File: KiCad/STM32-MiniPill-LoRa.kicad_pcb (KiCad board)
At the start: 2 copper layers, 51.3 x 28.8 mm, 6 parts, among them U1 STM32L051C8Tx, U2 RFM95W-868S2

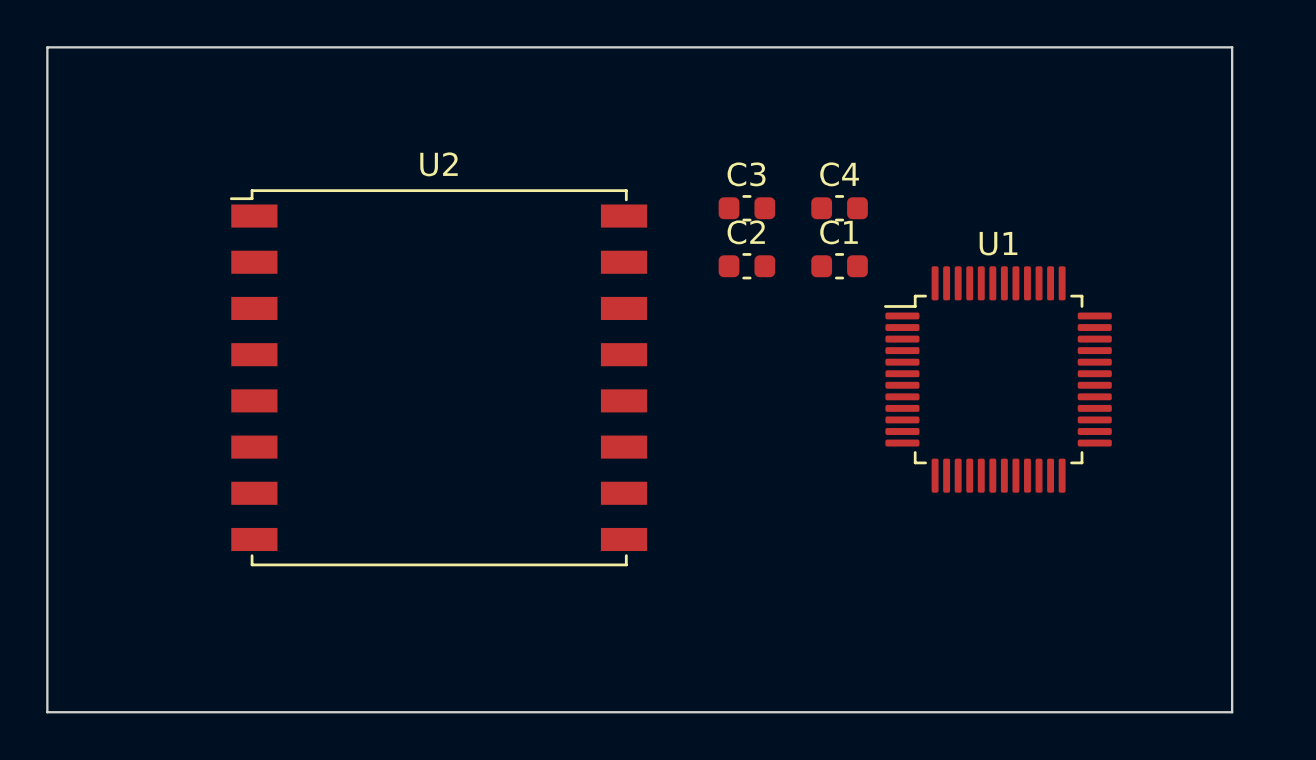
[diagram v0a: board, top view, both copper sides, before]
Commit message: adding ST-Link Connector
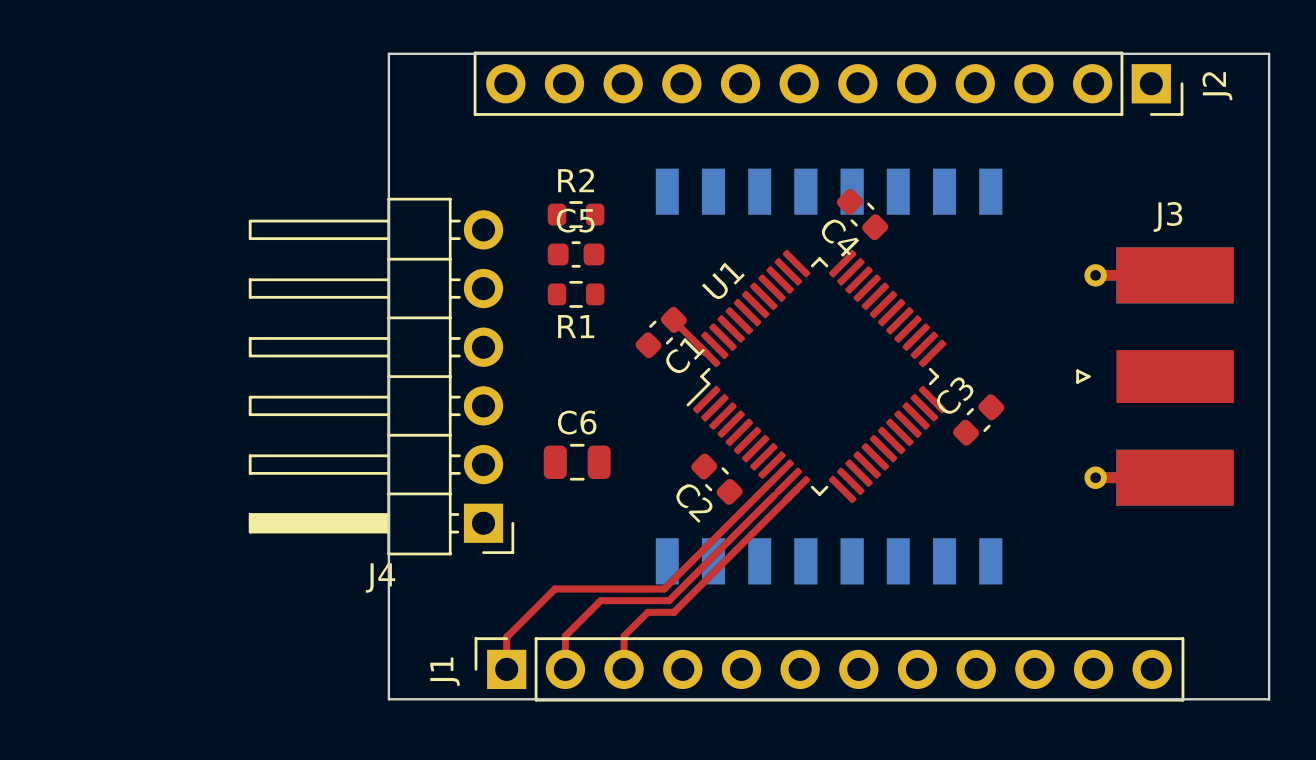
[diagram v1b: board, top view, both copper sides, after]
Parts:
- added C5: 100nF, Capacitor_SMD:C_0603_1608Metric, F.Cu at (144.6, 92.5)
- added C6: 10uF, Capacitor_SMD:C_0805_2012Metric, F.Cu at (144.7, 101.5)
- added J1: Conn_01x12_Female, Connector_PinSocket_2.54mm:PinSocket_1x12_P2.54mm_Vertical, F.Cu at (141.6, 110.5)
- added J2: Conn_01x12_Female, Connector_PinSocket_2.54mm:PinSocket_1x12_P2.54mm_Vertical, F.Cu at (169.5, 85.1)
- added J3: Conn_Coaxial, Connector_Coaxial:SMA_Molex_73251-1153_EdgeMount_Horizontal, F.Cu at (168.8, 97.8)
- added J4: Conn_01x06_Male, Connector_PinHeader_2.54mm:PinHeader_1x06_P2.54mm_Horizontal, F.Cu at (140.6, 104.1)
- added R1: 100K, Resistor_SMD:R_0603_1608Metric, F.Cu at (144.6, 94.2)
- added R2: 100K, Resistor_SMD:R_0603_1608Metric, F.Cu at (144.6, 90.8)
- C1, C2, C3, C4: value C -> 100nF
- U2: moved to B.Cu
- moved U2 16.9 mm to (155.6, 97.8), turned to -90 degrees
- moved C3 13.6 mm to (162.1, 99.7), turned to 45 degrees
- moved C2 9.31 mm to (150.7, 102.2), turned to 135 degrees
- moved C1 8.24 mm to (148.3, 95.9), turned to -135 degrees
- moved U1 7.75 mm to (155.2, 97.8), turned to 45 degrees
- moved C4 1.03 mm to (157.0, 90.8), turned to 135 degrees
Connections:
- U1 pad 10: unconnected-(U1-Pad10) -> /PA0
- U1 pad 11: unconnected-(U1-Pad11) -> /PA1
- U1 pad 12: unconnected-(U1-Pad12) -> /PA2
- U1 pad 13: unconnected-(U1-Pad13) -> /PA3
- U1 pad 14: unconnected-(U1-Pad14) -> /NSS
- U1 pad 15: unconnected-(U1-Pad15) -> /SCK
- U1 pad 16: unconnected-(U1-Pad16) -> /MISO
- U1 pad 17: unconnected-(U1-Pad17) -> /MOSI
- U1 pad 21: unconnected-(U1-Pad21) -> /PB10
- U1 pad 22: unconnected-(U1-Pad22) -> /PB11
- U1 pad 29: unconnected-(U1-Pad29) -> /PA8
- U1 pad 30: unconnected-(U1-Pad30) -> /RESET
- U1 pad 31: unconnected-(U1-Pad31) -> /DIO0
- U1 pad 34: unconnected-(U1-Pad34) -> /SWDIO
- U1 pad 37: unconnected-(U1-Pad37) -> /SWCLK
- U1 pad 40: unconnected-(U1-Pad40) -> /DIO1
- U1 pad 41: unconnected-(U1-Pad41) -> /DIO2
- U1 pad 42: unconnected-(U1-Pad42) -> /PB6
- U1 pad 43: unconnected-(U1-Pad43) -> /PB7
- U1 pad 44: unconnected-(U1-Pad44) -> Net-(R2-Pad1)
- U1 pad 45: unconnected-(U1-Pad45) -> /PB8
- U1 pad 46: unconnected-(U1-Pad46) -> /PB9
- U1 pad 7: unconnected-(U1-Pad7) -> /NRST
- U2 pad 1: unconnected-(U2-Pad1) -> GND
- U2 pad 10: unconnected-(U2-Pad10) -> GND
- U2 pad 13: unconnected-(U2-Pad13) -> +3.3V
- U2 pad 14: unconnected-(U2-Pad14) -> /DIO0
- U2 pad 15: unconnected-(U2-Pad15) -> /DIO1
- U2 pad 16: unconnected-(U2-Pad16) -> /DIO2
- U2 pad 2: unconnected-(U2-Pad2) -> /MISO
- U2 pad 3: unconnected-(U2-Pad3) -> /MOSI
- U2 pad 4: unconnected-(U2-Pad4) -> /SCK
- U2 pad 5: unconnected-(U2-Pad5) -> /NSS
- U2 pad 6: unconnected-(U2-Pad6) -> /RESET
- U2 pad 8: unconnected-(U2-Pad8) -> GND
- U2 pad 9: unconnected-(U2-Pad9) -> Net-(J3-Pad1)
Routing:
- net /PA0: track 0.00 -> 15.4 mm
- net /PA1: track 0.00 -> 13.0 mm
- net /PA2: track 0.00 -> 11.5 mm
- net +3.3V: track 0.00 -> 2.04 mm
- added copper zone on B.Cu, net GND
- added copper zone on F.Cu, net GND
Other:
- board size 51.3 x 28.8 mm -> 38.1 x 27.9 mm

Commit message: adding 3D Models of SMA Molex Connector
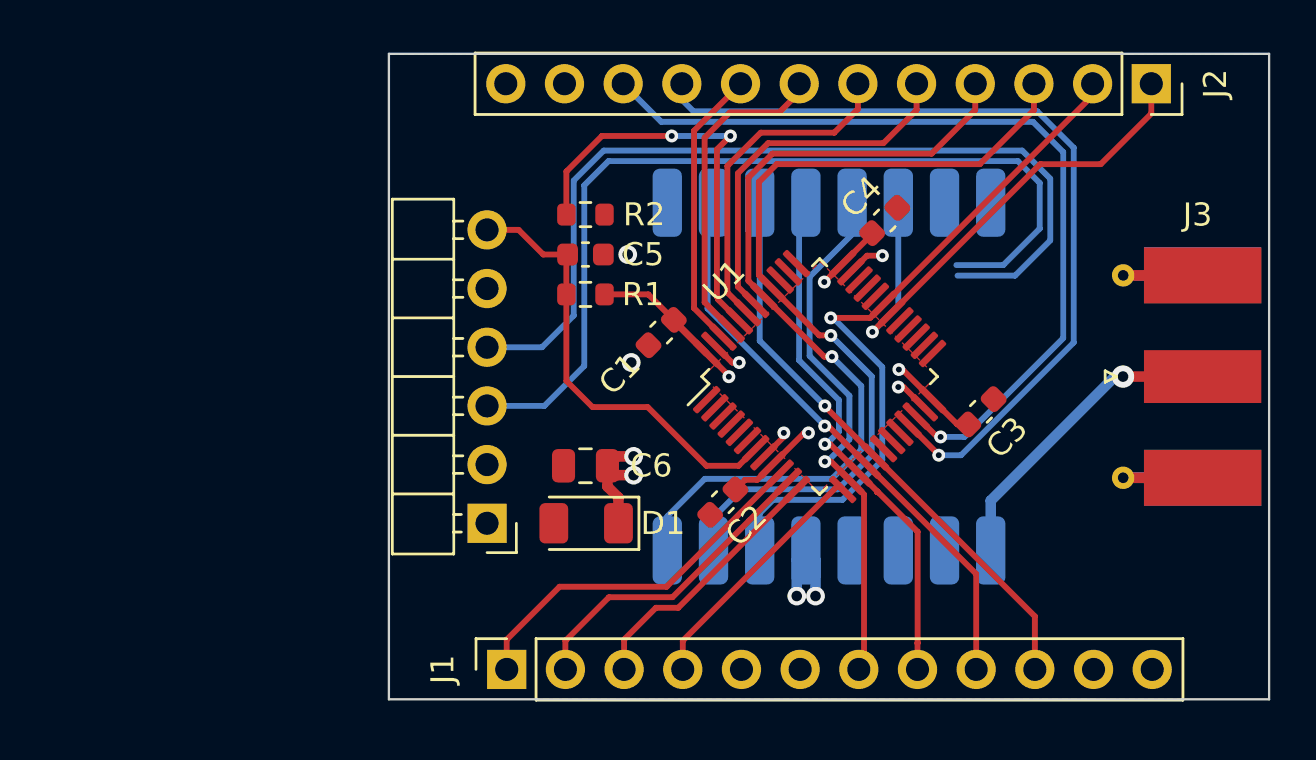
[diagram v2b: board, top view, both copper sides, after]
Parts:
- added D1: D, Diode_SMD:D_1206_3216Metric, F.Cu at (145.1, 104.1)
- moved J3 1.19 mm to (170.0, 97.8)
- moved C2 1.02 mm to (151.0, 103.2), turned to -135 degrees
- moved C4 1.00 mm to (158.0, 91.0), turned to 45 degrees
- moved C5 0.41 mm to (145.0, 92.5)
- moved R1 0.41 mm to (145.0, 94.2)
- moved R2 0.41 mm to (145.0, 90.8)
- moved C6 0.39 mm to (145.0, 101.7), turned to 180 degrees
- moved C3 0.37 mm to (162.2, 99.3)
- moved J4 0.15 mm to (140.8, 104.1)
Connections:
- J1 pad 11: VCC -> +3.3V
- J1 pad 5: VCC -> +3.3V
- J2 pad 1: /PA9 -> /RESET
- J2 pad 12: VCC -> +3.3V
- J4 pad 1: VCC -> +3.3V
- J4 pad 5: VCC -> +3.3V
- U1 pad 29: /PA8 -> unconnected-(U1-PA8-Pad29)
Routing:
- net +3.3V: track 2.04 -> 83.6 mm, vias 0 -> 8
- net /SWCLK: track 0.00 -> 39.5 mm
- net /SWDIO: track 0.00 -> 39.1 mm
- net /DIO1: track 0.00 -> 37.9 mm, vias 0 -> 1
- net /DIO2: track 0.00 -> 37.2 mm, vias 0 -> 1
- net /PB11: track 0.00 -> 36.8 mm, vias 0 -> 1
- net /PB10: track 0.00 -> 36.7 mm, vias 0 -> 1
- net /DIO0: track 0.00 -> 30.8 mm, vias 0 -> 1
- net /MISO: track 0.00 -> 25.2 mm, vias 0 -> 1
- net /MOSI: track 0.00 -> 25.1 mm, vias 0 -> 1
- net /RESET: track 0.00 -> 23.3 mm, vias 0 -> 1
- net /SCK: track 0.00 -> 23.1 mm, vias 0 -> 1
- net /NSS: track 0.00 -> 23.1 mm, vias 0 -> 1
- net /NRST: track 0.00 -> 19.4 mm
- net Net-(U1-BOOT0): track 0.00 -> 18.2 mm, vias 0 -> 2
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- added copper zone on F.Cu, net +3.3V
- added copper zone on In1.Cu, net +3.3V
- added copper zone on In2.Cu, net GND
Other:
- copper layers 2 -> 4

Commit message: first time every trace routed
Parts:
- moved C4 0.29 mm to (157.8, 90.8)
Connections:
- J1 pad 11: +3.3V -> VCC
- J1 pad 5: +3.3V -> VCC
- J2 pad 12: +3.3V -> VCC
- J4 pad 1: +3.3V -> VCC
- J4 pad 5: +3.3V -> VCC
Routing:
- net VCC: track 0.00 -> 58.9 mm, vias 0 -> 1
- net +3.3V: track 83.6 -> 27.7 mm
- net /SWCLK: track 39.5 -> 50.5 mm, vias 0 -> 1
- net GND: track 5.91 -> 11.1 mm, vias 6 -> 10
- net /PB10: track 36.7 -> 37.7 mm
- net /PB11: track 36.8 -> 37.8 mm
- net /DIO0: track 30.8 -> 31.6 mm
- net /DIO1: track 37.9 -> 37.1 mm
- net /DIO2: track 37.2 -> 36.7 mm
- net /SWDIO: track 39.1 -> 39.4 mm, vias 0 -> 1
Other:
- board text added: "A0"
- board text added: "A1"
- board text added: "A10"
- board text added: "A2"
- board text added: "A3"
- board text added: "A4"
- board text added: "A5"
- board text added: "A6"
- board text added: "A7"
- board text added: "A9"
- board text added: "B10"
- board text added: "B11"
- board text added: "B4"
- board text added: "B5"
- board text added: "B6"
- board text added: "B7"
- board text added: "B8"
- board text added: "B9"
- board text added: "GND"
- board text added: "VCC"

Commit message: last modification before push to GitHub
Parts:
- added REF**: MountingHole_2.2mm_M2_DIN965, MountingHole:MountingHole_2.2mm_M2_DIN965, F.Cu at (138.2, 110.1)
- added REF**: MountingHole_2.2mm_M2_DIN965, MountingHole:MountingHole_2.2mm_M2_DIN965, F.Cu at (173.0, 85.5)
- added REF**: MountingHole_2.2mm_M2_DIN965, MountingHole:MountingHole_2.2mm_M2_DIN965, F.Cu at (173.0, 110.1)
- added REF**: MountingHole_2.2mm_M2_DIN965, MountingHole:MountingHole_2.2mm_M2_DIN965, F.Cu at (138.2, 85.5)
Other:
- board text added: "G"
- board text added: "ST-LINK"
- board text added: "V"
- board text added: "locked"

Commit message: fist order
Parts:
- removed D1: D, Diode_SMD:D_1206_3216Metric
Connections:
- C1 pad 1: +3.3V -> VCC
- C2 pad 1: +3.3V -> VCC
- C3 pad 1: +3.3V -> VCC
- C4 pad 1: +3.3V -> VCC
- C6 pad 1: +3.3V -> VCC
- R1 pad 1: +3.3V -> VCC
- U1 pad 24: +3.3V -> VCC
- U1 pad 36: +3.3V -> VCC
- U1 pad 48: +3.3V -> VCC
- U1 pad 9: +3.3V -> VCC
- U2 pad 13: +3.3V -> VCC
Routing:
- net +3.3V: track 27.7 -> 0.00 mm, vias 8 -> 0
- net VCC: track 58.9 -> 31.7 mm, vias 1 -> 8
- added copper zone on F.Cu, net VCC
- added copper zone on In1.Cu, net VCC
- removed copper zone on F.Cu, net +3.3V
- removed copper zone on In1.Cu, net +3.3V
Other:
- outline, holes or cut-outs redrawn
